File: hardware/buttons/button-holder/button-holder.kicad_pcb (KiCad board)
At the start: 2 copper layers, 27 x 28 mm, 6 parts, among them J1 Conn_01x02, SW1 SW_SPST

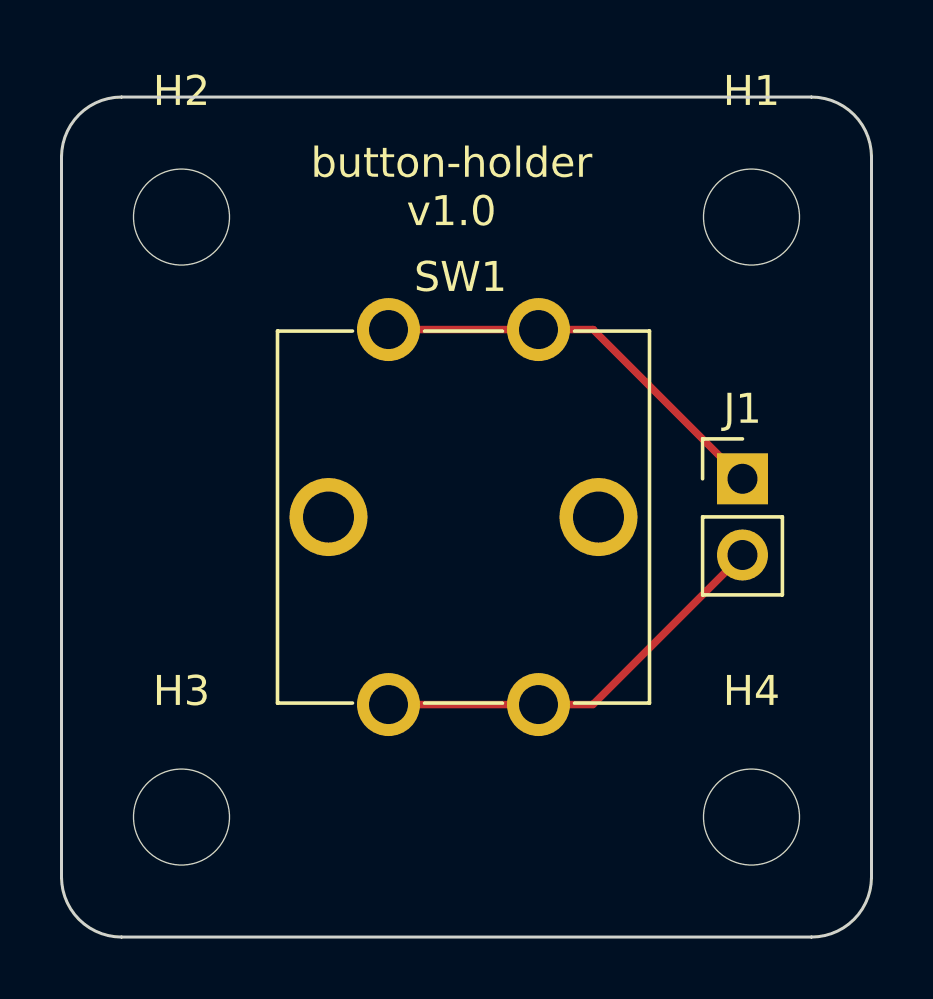
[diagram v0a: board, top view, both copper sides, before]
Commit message: Fix button holder pinout
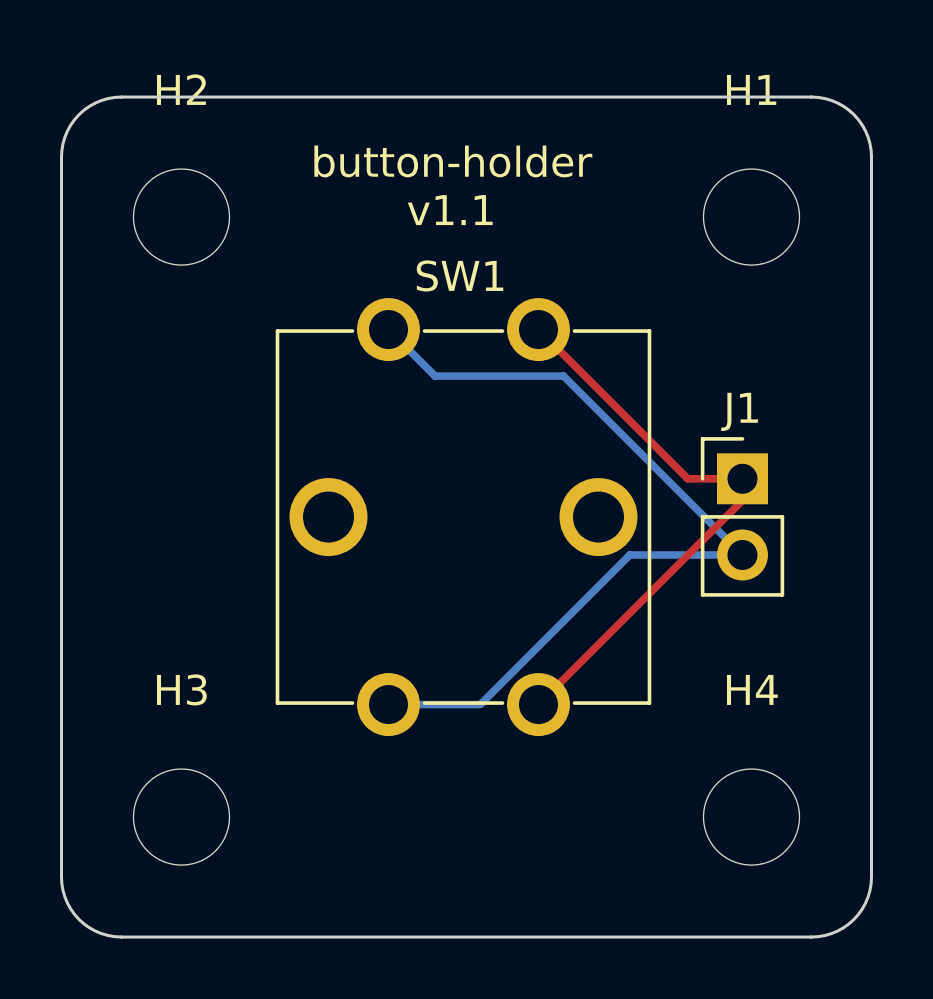
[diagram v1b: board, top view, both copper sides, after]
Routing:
- net Net-(J1-Pad2): track 13.9 -> 28.8 mm
- net Net-(J1-Pad1): track 13.9 -> 19.2 mm
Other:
- board text added: "button-holder v1.1"
- board text removed: "button-holder v1.0"
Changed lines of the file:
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@@
       (effects (font (size 1 1) (thickness 0.15)))
     )
-    (fp_line (start 8.7 12.45) (end 6.2 12.45) (layer "F.SilkS") (width 0.12))
-    (fp_line (start 3.8 12.45) (end 1.2 12.45) (layer "F.SilkS") (width 0.12))
-    (fp_line (start -1.2 12.45) (end -3.7 12.45) (layer "F.SilkS") (width 0.12))
-    (fp_line (start -3.7 0.05) (end -1.2 0.05) (layer "F.SilkS") (width 0.12))
-    (fp_line (start 8.7 0.05) (end 8.7 12.45) (layer "F.SilkS") (width 0.12))
-    (fp_line (start 1.2 0.05) (end 3.8 0.05) (layer "F.SilkS") (width 0.12))
     (fp_line (start 6.2 0.05) (end 8.7 0.05) (layer "F.SilkS") (width 0.12))
     (fp_line (start -3.7 12.45) (end -3.7 0.05) (layer "F.SilkS") (width 0.12))
+    (fp_line (start 1.2 0.05) (end 3.8 0.05) (layer "F.SilkS") (width 0.12))
+    (fp_line (start 3.8 12.45) (end 1.2 12.45) (layer "F.SilkS") (width 0.12))
+    (fp_line (start -3.7 0.05) (end -1.2 0.05) (layer "F.SilkS") (width 0.12))
+    (fp_line (start 8.7 12.45) (end 6.2 12.45) (layer "F.SilkS") (width 0.12))
+    (fp_line (start 8.7 0.05) (end 8.7 12.45) (layer "F.SilkS") (width 0.12))
+    (fp_line (start -1.2 12.45) (end -3.7 12.45) (layer "F.SilkS") (width 0.12))
     (fp_rect (start -3.75 0) (end 8.75 12.5) (layer "F.CrtYd") (width 0.05) (fill none))
     (fp_rect (start -3.5 0.25) (end 8.5 12.25) (layer "F.Fab") (width 0.1) (fill none))
-    (pad "1" thru_hole circle (at 0 0) (size 2.1 2.1) (drill 1.3) (layers *.Cu *.Mask)
+    (pad "1" thru_hole circle (at 5 12.5) (size 2.1 2.1) (drill 1.3) (layers *.Cu *.Mask)
       (net 1 "Net-(J1-Pad1)") (pinfunction "A") (pintype "passive"))
     (pad "1" thru_hole circle (at 5 0) (size 2.1 2.1) (drill 1.3) (layers *.Cu *.Mask)
       (net 1 "Net-(J1-Pad1)") (pinfunction "A") (pintype "passive"))
-    (pad "2" thru_hole circle (at 5 12.5) (size 2.1 2.1) (drill 1.3) (layers *.Cu *.Mask)
+    (pad "2" thru_hole circle (at 0 0) (size 2.1 2.1) (drill 1.3) (layers *.Cu *.Mask)
       (net 2 "Net-(J1-Pad2)") (pinfunction "B") (pintype "passive"))
     (pad "2" thru_hole circle (at 0 12.5) (size 2.1 2.1) (drill 1.3) (layers *.Cu *.Mask)
@@
   (gr_arc (start 108 67) (mid 107.414214 68.414214) (end 106 69) (layer "Edge.Cuts") (width 0.1))
   (gr_line (start 83 41) (end 106 41) (layer "Edge.Cuts") (width 0.1))
-  (gr_text "button-holder\nv1.0" (at 95 44) (layer "B.SilkS")
+  (gr_text "button-holder\nv1.1" (at 95 44) (layer "B.SilkS")
     (effects (font (size 1 1) (thickness 0.15)) (justify mirror))
   )
-  (gr_text "button-holder\nv1.0" (at 94 44) (layer "F.SilkS")
+  (gr_text "button-holder\nv1.1" (at 94 44) (layer "F.SilkS")
     (effects (font (size 1 1) (thickness 0.15)))
   )
-  (segment (start 96.9 48.75) (end 98.725 48.75) (width 0.25) (layer "F.Cu") (net 1))
-  (segment (start 91.9 48.75) (end 96.9 48.75) (width 0.25) (layer "F.Cu") (net 1))
-  (segment (start 98.725 48.75) (end 103.7 53.725) (width 0.25) (layer "F.Cu") (net 1))
-  (segment (start 96.9 61.25) (end 98.715 61.25) (width 0.25) (layer "F.Cu") (net 2))
-  (segment (start 98.715 61.25) (end 103.7 56.265) (width 0.25) (layer "F.Cu") (net 2))
-  (segment (start 91.9 61.25) (end 96.9 61.25) (width 0.25) (layer "F.Cu") (net 2))
+  (segment (start 103.7 53.725) (end 103.7 54.45) (width 0.25) (layer "F.Cu") (net 1))
+  (segment (start 103.7 53.725) (end 101.875 53.725) (width 0.25) (layer "F.Cu") (net 1))
+  (segment (start 101.875 53.725) (end 96.9 48.75) (width 0.25) (layer "F.Cu") (net 1))
+  (segment (start 103.7 54.45) (end 96.9 61.25) (width 0.25) (layer "F.Cu") (net 1))
+  (segment (start 103.7 56.265) (end 99.941147 56.265) (width 0.25) (layer "B.Cu") (net 2))
+  (segment (start 93.45 50.3) (end 91.9 48.75) (width 0.25) (layer "B.Cu") (net 2))
+  (segment (start 97.735 50.3) (end 93.45 50.3) (width 0.25) (layer "B.Cu") (net 2))
+  (segment (start 94.956147 61.25) (end 91.9 61.25) (width 0.25) (layer "B.Cu") (net 2))
+  (segment (start 103.7 56.265) (end 97.735 50.3) (width 0.25) (layer "B.Cu") (net 2))
+  (segment (start 99.941147 56.265) (end 94.956147 61.25) (width 0.25) (layer "B.Cu") (net 2))
 )
